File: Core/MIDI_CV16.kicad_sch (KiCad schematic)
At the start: 106 parts, among them J1 USB_C_Receptacle_USB2.0, J2 Conn_01x06_Male, J3 Conn_01x10_Female, J5 Conn_01x04, J7 Conn_01x10_Female, SW1 SW_Push_DPDT, U1 ATSAMD21G17D, U10 TL072, U11 TL072, U12 TL072, U13 MCP2517FD-xSL, U14 TLE9250V, U2 CD4052, U4 TL072, U5 TL072, U6 TL072, U7 TL072, U8 CD4052, U9 TL072, Y1 20MHz

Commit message: Update PCBs to V3.0
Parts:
- removed C10, C11, C12, C13, C14, C15, C17, C18, C19, C20, C21, C22, C23, C24, C4, C6, C7, C8, C9: 100nF, Capacitor_SMD:C_0603_1608Metric, symbol Device:C
- removed J3, J7: Conn_01x10_Female, Custom_FP:PinSocket_1x10_P2.54mm_Vertical_SMD_Pin1Both, symbol Connector:Conn_01x10_Socket
- removed R10, R13, R15, R18, R20, R21, R33, R36, R38, R40, R42, R44, R46, R48, R6, R8: 200k, Resistor_SMD:R_0603_1608Metric, symbol Device:R
- removed R11, R14, R17, R19, R25, R32, R34, R37, R39, R41, R43, R45, R47, R5, R7, R9: 68k, Resistor_SMD:R_0603_1608Metric, symbol Device:R
- removed R12, R16, R51, R52: 16k, Resistor_SMD:R_0603_1608Metric, symbol Device:R
- removed R22, R23, R26, R27, R29, R30, R31, R35, R49, R50, R53, R54, R55, R56, R57, R58: 110k, Resistor_SMD:R_0603_1608Metric, symbol Device:R
- removed U1: ATSAMD21G17D, Package_QFP:TQFP-48_7x7mm_P0.5mm, symbol MCU_Microchip_SAMD:ATSAMD21G17D-A
- removed U10, U11, U12, U4, U5, U6, U7, U9: TL072, Package_SO:SOIC-8_3.9x4.9mm_P1.27mm, symbol Amplifier_Operational:TL072
- removed U2, U8: CD4052, Package_SO:SOIC-16_3.9x9.9mm_P1.27mm, symbol Analog_Switch:CD4052B
- added C54, C55: 100nF, Capacitor_SMD:C_0603_1608Metric, symbol Device:C
- added C60, C61: 27pF, Capacitor_SMD:C_0603_1608Metric, symbol Device:C
- added R61, R62: 27.4, Resistor_SMD:R_0603_1608Metric, symbol Device:R
- added R64, R66: 1k, Resistor_SMD:R_0603_1608Metric, symbol Device:R
- added R65: NC, Resistor_SMD:R_0603_1608Metric, symbol Device:R
- added SW2, SW3: SW_SPST, Custom_FP:Tactile_angled_5x5.4_SMD, symbol Switch:SW_SPST
- added U1: RP2040, Package_DFN_QFN:QFN-56-1EP_7x7mm_P0.4mm_EP3.2x3.2mm, symbol MCU_RaspberryPi:RP2040
- added U16: CAT25640, Package_SO:SO-8_3.9x4.9mm_P1.27mm, symbol Memory_EEPROM:CAT250xxx
- added U17: IS25LP032D, Package_SO:SOIC-8_3.9x4.9mm_P1.27mm, symbol Memory_Flash:AT25SF081-SSHD-X
- added Y2: ECS-120-18-33-JGN-TR3, Crystal:Crystal_SMD_3225-4Pin_3.2x2.5mm_HandSoldering, symbol Device:Crystal_GND24
- C1: value 100nF -> 1µF
- J2: footprint Connector_PinHeader_2.54mm:PinHeader_2x03_P2.54mm_Vertical_SMD -> Custom_FP:TSM103-DH
- J5: footprint Custom_FP:MicroMatch_04_Vertical_SMD -> Custom_FP:MicroMatch_04_Vertical_SMD_Lock
- R28, R59: value 56 -> 62
- R4: value 10k -> NC
- R60: value 1k -> NC
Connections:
- net +3V3: now also R65.1, U1.1 (IOVDD), U1.10 (IOVDD), U1.22 (IOVDD), U1.33 (IOVDD), U1.42 (IOVDD), U1.43 (ADC_AVDD), U1.44 (VREG_IN), U1.48 (USB_VDD), U1.49 (IOVDD), U16.3 (~{WP}), U16.7 (~{HOLD}), U16.8 (VCC), U17.8 (VCC)
- net Butt1: now also U1.4 (GPIO2)
- net Butt2: now also U1.3 (GPIO1)
- net Butt3: now also U1.2 (GPIO0)
- net CAN_INT: now also U1.36 (GPIO24)
- net GND: now also C54.2, C55.2, C60.1, C61.1, SW2.1 (A), SW3.1 (A), U1.19 (TESTEN), U1.57 (GND), U16.4 (GND), U17.4 (GND), Y2.2, Y2.4
- net LEDC1: now also U1.15 (GPIO12)
- net LEDC2: now also U1.16 (GPIO13)
- net LEDC3: now also U1.17 (GPIO14)
- net LEDC4: now also U1.18 (GPIO15)
- net LEDC5: now also U1.28 (GPIO17)
- net LEDC6: now also U1.29 (GPIO18)
- net LEDC7: now also U1.30 (GPIO19)
- net LEDC8: now also U1.37 (GPIO25)
- net LEDR1: now also U1.41 (GPIO29_ADC3)
- net LEDR2: now also U1.40 (GPIO28_ADC2)
- net LEDR3: now also U1.39 (GPIO27_ADC1)
- net LEDR4: now also U1.38 (GPIO26_ADC0)
- net LEDR5: now also U1.27 (GPIO16)
- net MUX_A: now also U1.7 (GPIO5)
- net MUX_B: now also U1.6 (GPIO4)
- net MUX_INH: now also U1.8 (GPIO6)
- net RESET: now also SW3.2 (B), U1.26 (RUN)
- net SPI_MISO: now also U1.11 (GPIO8), U16.2 (MISO); no longer U13.12 (SDO)
- net SPI_MOSI: now also U1.14 (GPIO11), U16.5 (MOSI); no longer U13.11 (SDI)
- net SPI_SCK: now also U1.13 (GPIO10), U16.6 (SCK); no longer U13.10 (SCK)
- net SWCLK: now also U1.24 (SWCLK)
- net SWDIO: now also U1.25 (SWD)
- net USB_D+: now also R61.1
- net USB_D-: now also R62.2
- net at C3.1: now also C54.1, C55.1, U1.23 (DVDD), U1.45 (VREG_VOUT), U1.50 (DVDD)
- net MIDIBUS+ renamed M2IDI+
- net MIDIBUS- renamed M2IDI-
- net SPI_SS renamed CAN_CS
- net CAN_CS: now also U1.32 (GPIO21)
- new net: C60.2, R66.1, Y2.1
- new net: R66.2, U1.21 (XOUT)
- new net: R64.2, SW2.2 (B)
- new net: C61.2, U1.20 (XIN), Y2.3
- new net CAN_MISO: U1.31 (GPIO20), U13.12 (SDO)
- new net CAN_MOSI: U1.35 (GPIO23), U13.11 (SDI)
- new net CAN_SCK: U1.34 (GPIO22), U13.10 (SCK)
- new net DAC_CS: U1.9 (GPIO7)
- new net EEPROM_CS: U1.12 (GPIO9), U16.1 (~{CS})
- new net FLASH_CS: R64.1, R65.2, U1.56 (QSPI_SS), U17.1 (~{CS})
- new net FLASH_SCK: U1.52 (QSPI_SCLK), U17.6 (SCK)
- new net FLASH_SD0: U1.53 (QSPI_SD0), U17.5 (SI/IO0)
- new net FLASH_SD1: U1.55 (QSPI_SD1), U17.2 (SO/IO1)
- new net FLASH_SD2: U1.54 (QSPI_SD2), U17.3 (~{WP}/IO2)
- new net FLASH_SD3: U1.51 (QSPI_SD3), U17.7 (~{HOLD}/IO3)
- new net MCU_USB_D+: R61.2, U1.47 (USB_DP)
- new net MCU_USB_D-: R62.1, U1.46 (USB_DM)
- no-connect marks 4 -> 5
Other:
- added sheet Outputs (Outputs.kicad_sch)
- note removed: "31k"
- note removed: "47k"
- note removed: "91k"
- note removed: "TxD on SERCOM[0] or SERCOM[2]"
- moved on the sheet: C3, J2, R4, R60

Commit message: Shrink crystal fp and add silkscreen text
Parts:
- Y2: footprint Crystal:Crystal_SMD_3225-4Pin_3.2x2.5mm_HandSoldering -> Custom_FP:Crystal_SMD_3225-4Pin_3.2x2.5mm_HandSoldering
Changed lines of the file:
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@@
       (effects (font (size 1.27 1.27)))
     )
-    (property "Footprint" "Crystal:Crystal_SMD_3225-4Pin_3.2x2.5mm_HandSoldering" (at 85.725 139.065 0)
+    (property "Footprint" "Custom_FP:Crystal_SMD_3225-4Pin_3.2x2.5mm_HandSoldering" (at 85.725 139.065 0)
       (effects (font (size 1.27 1.27)) hide)
     )

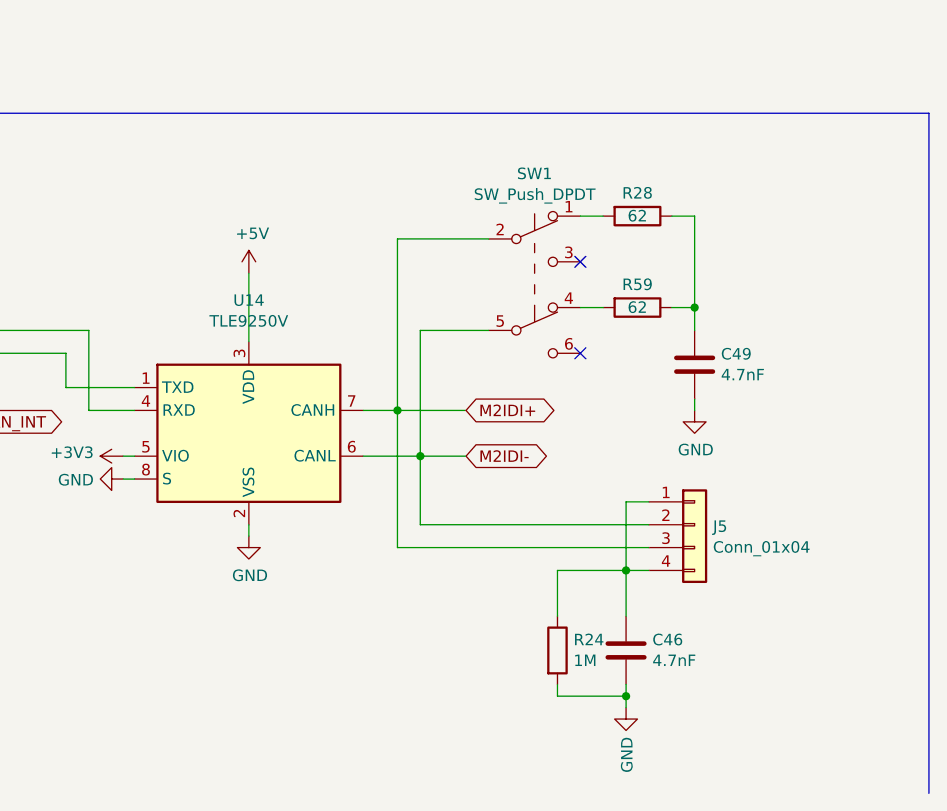
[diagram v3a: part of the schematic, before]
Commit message: Change CAN tranceiver to MCP2562
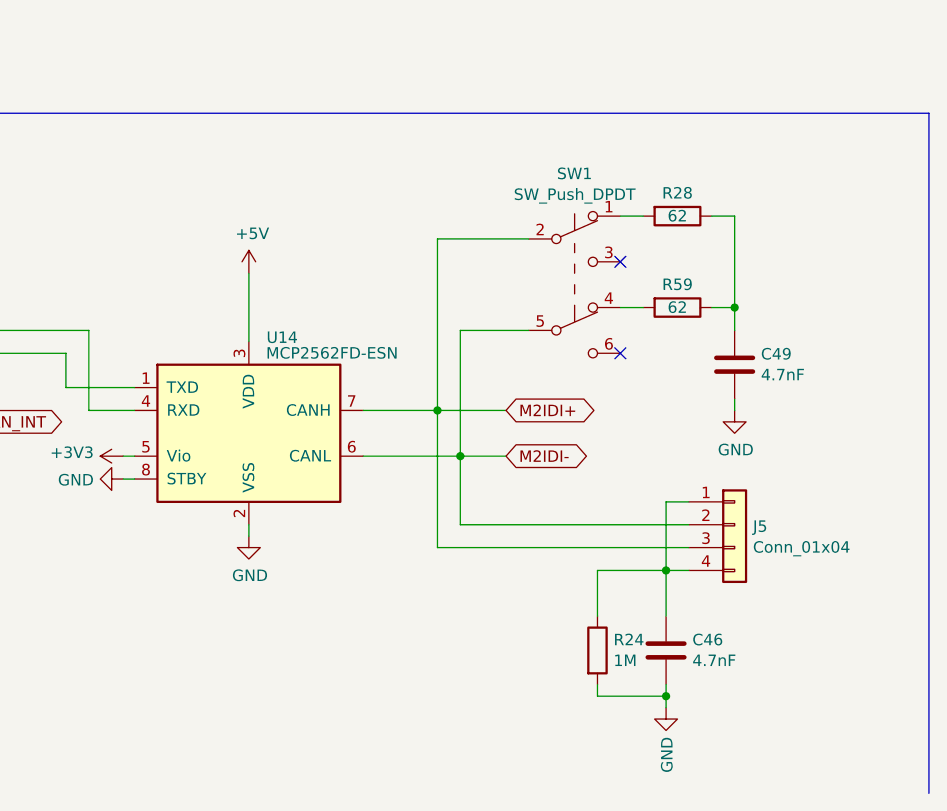
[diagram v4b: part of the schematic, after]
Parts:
- removed U14: TLE9250V, Package_SO:Infineon_PG-DSO-8-27_3.9x4.9mm_EP2.65x3mm, symbol Interface_CAN_LIN:MCP2558FD-xMF
- added U14: MCP2562FD-ESN, Package_SO:SOIC-8_3.9x4.9mm_P1.27mm, symbol Interface_CAN_LIN:MCP2562-E-SN
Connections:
- net +3V3: now also U14.5 (Vio)
- net +5V: now also U14.3 (VDD)
- net GND: now also U14.2 (VSS), U14.8 (STBY)
- net M2IDI+: now also U14.7 (CANH)
- net M2IDI-: now also U14.6 (CANL)
- net at U13.1 (TXCAN): now also U14.1 (TXD)
- net at U13.2 (RXCAN): now also U14.4 (RXD)
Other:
- moved on the sheet: C46, C49, J5, R24, R28, R59, SW1

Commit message: Finalize module
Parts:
- R28, R59: footprint Resistor_SMD:R_0603_1608Metric -> Resistor_SMD:R_0805_2012Metric
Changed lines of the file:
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@@
       (effects (font (size 1.27 1.27)))
     )
-    (property "Footprint" "Resistor_SMD:R_0603_1608Metric" (at 244.475 229.362 90)
+    (property "Footprint" "Resistor_SMD:R_0805_2012Metric" (at 244.475 229.362 90)
       (effects (font (size 1.27 1.27)) hide)
     )
@@
       (effects (font (size 1.27 1.27)))
     )
-    (property "Footprint" "Resistor_SMD:R_0603_1608Metric" (at 244.475 219.202 90)
+    (property "Footprint" "Resistor_SMD:R_0805_2012Metric" (at 244.475 219.202 90)
       (effects (font (size 1.27 1.27)) hide)
     )

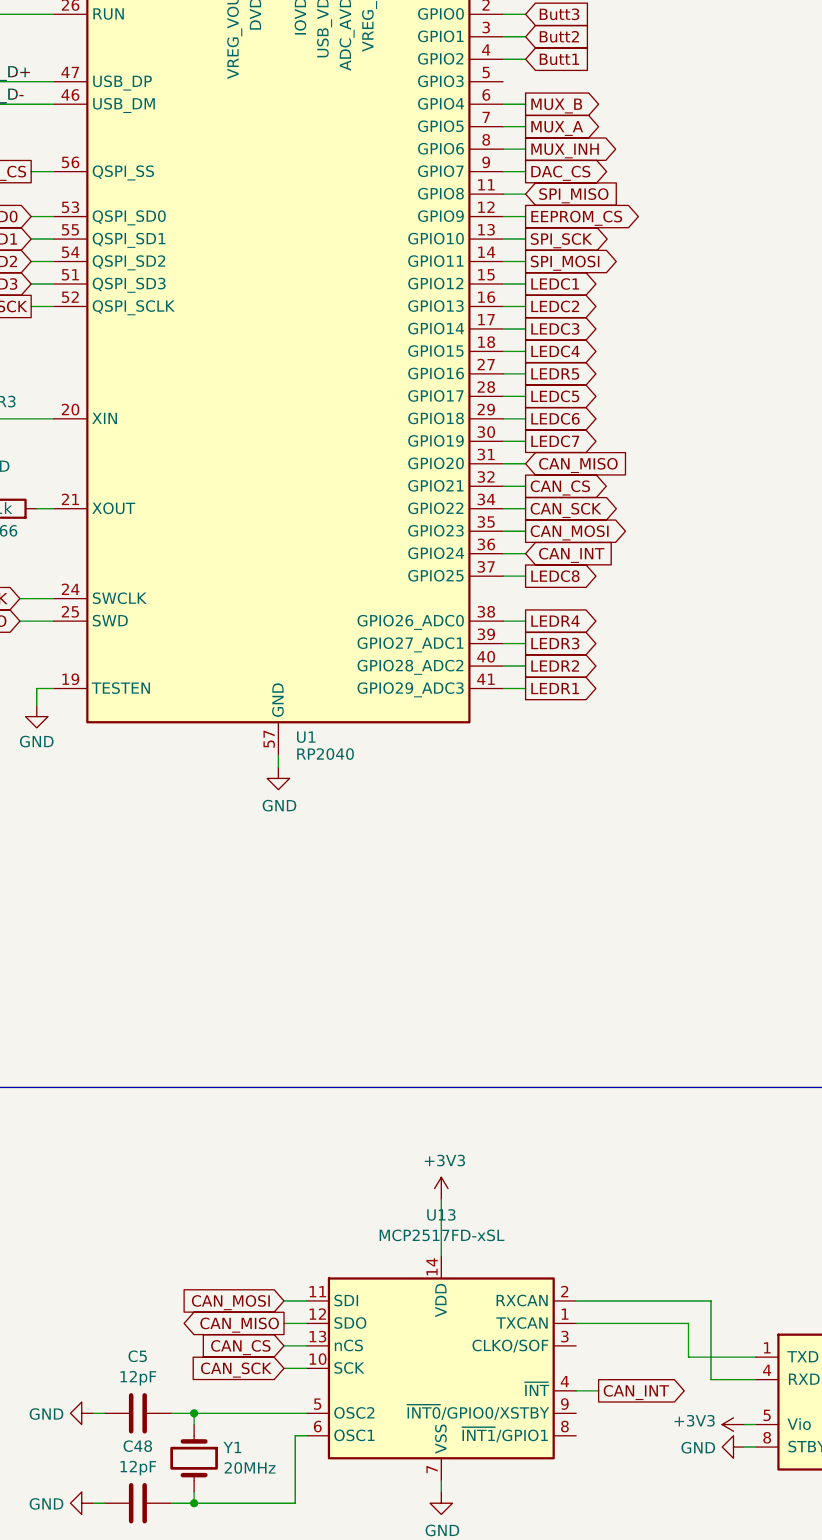
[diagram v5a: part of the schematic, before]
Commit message: Change SPI bus for EEPROM
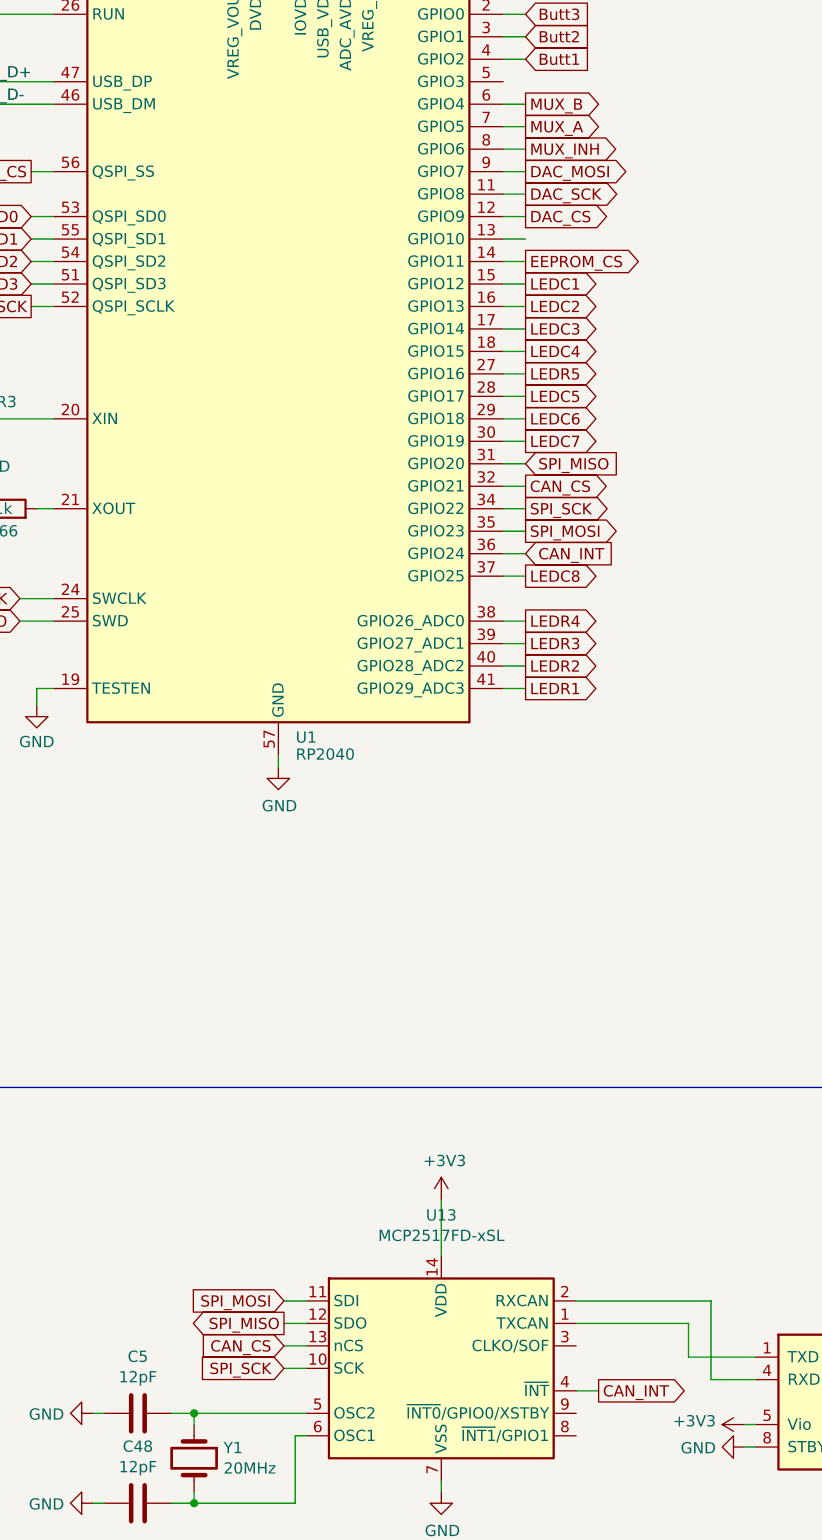
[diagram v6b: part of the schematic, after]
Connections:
- net CAN_MISO is gone; now on net SPI_MISO: U1.31 (GPIO20), U13.12 (SDO)
- net CAN_MOSI is gone; now on net SPI_MOSI: U1.35 (GPIO23), U13.11 (SDI)
- net CAN_SCK is gone; now on net SPI_SCK: U1.34 (GPIO22), U13.10 (SCK)
- net DAC_CS: now also U1.12 (GPIO9); no longer U1.9 (GPIO7)
- net EEPROM_CS: now also U1.14 (GPIO11); no longer U1.12 (GPIO9)
- net SPI_MISO: no longer U1.11 (GPIO8)
- net SPI_MOSI: no longer U1.14 (GPIO11)
- net SPI_SCK: no longer U1.13 (GPIO10)
- new net DAC_MOSI: U1.9 (GPIO7)
- new net DAC_SCK: U1.11 (GPIO8)
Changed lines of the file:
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@@
     (effects (font (size 1.27 1.27)) (justify left bottom))
   )
-  (global_label "SPI_SCK" (shape output) (at 158.115 113.665 0) (fields_autoplaced)
-    (effects (font (size 1.27 1.27)) (justify left))
-    (property "Intersheetrefs" "${INTERSHEET_REFS}" (at 168.168 113.665 0)
+  (global_label "DAC_SCK" (shape output) (at 158.115 108.585 0) (fields_autoplaced)
+    (effects (font (size 1.27 1.27)) (justify left))
+    (property "Intersheetrefs" "${INTERSHEET_REFS}" (at 168.7917 108.585 0)
       (effects (font (size 1.27 1.27)) (justify left) hide)
     )
@@
     )
   )
-  (global_label "SPI_MISO" (shape input) (at 158.115 108.585 0) (fields_autoplaced)
-    (effects (font (size 1.27 1.27)) (justify left))
-    (property "Intersheetrefs" "${INTERSHEET_REFS}" (at 169.0147 108.585 0)
-      (effects (font (size 1.27 1.27)) (justify left) hide)
-    )
-  )
   (global_label "SWDIO" (shape output) (at 35.56 192.405 180)
     (effects (font (size 1.27 1.27)) (justify right))
@@
     )
   )
-  (global_label "DAC_CS" (shape output) (at 158.115 106.045 0) (fields_autoplaced)
-    (effects (font (size 1.27 1.27)) (justify left))
-    (property "Intersheetrefs" "${INTERSHEET_REFS}" (at 167.4423 106.045 0)
-      (effects (font (size 1.27 1.27)) (justify left) hide)
-    )
-  )
-  (global_label "CAN_MISO" (shape output) (at 130.81 236.22 180)
+  (global_label "DAC_CS" (shape output) (at 158.115 111.125 0) (fields_autoplaced)
+    (effects (font (size 1.27 1.27)) (justify left))
+    (property "Intersheetrefs" "${INTERSHEET_REFS}" (at 167.4423 111.125 0)
+      (effects (font (size 1.27 1.27)) (justify left) hide)
+    )
+  )
+  (global_label "SPI_MISO" (shape output) (at 130.81 236.22 180)
     (effects (font (size 1.27 1.27)) (justify right))
     (property "Intersheetrefs" "${INTERSHEET_REFS}" (at 130.81 236.22 0)
@@
     )
   )
-  (global_label "CAN_MOSI" (shape input) (at 130.81 233.68 180)
+  (global_label "SPI_MOSI" (shape input) (at 130.81 233.68 180)
     (effects (font (size 1.27 1.27)) (justify right))
     (property "Intersheetrefs" "${INTERSHEET_REFS}" (at 130.81 233.68 0)
@@
     )
   )
-  (global_label "EEPROM_CS" (shape output) (at 158.115 111.125 0) (fields_autoplaced)
-    (effects (font (size 1.27 1.27)) (justify left))
-    (property "Intersheetrefs" "${INTERSHEET_REFS}" (at 171.4336 111.125 0)
+  (global_label "EEPROM_CS" (shape output) (at 158.115 116.205 0) (fields_autoplaced)
+    (effects (font (size 1.27 1.27)) (justify left))
+    (property "Intersheetrefs" "${INTERSHEET_REFS}" (at 171.4336 116.205 0)
       (effects (font (size 1.27 1.27)) (justify left) hide)
     )
@@
     )
   )
-  (global_label "CAN_SCK" (shape input) (at 130.81 241.3 180)
+  (global_label "SPI_SCK" (shape input) (at 130.81 241.3 180)
     (effects (font (size 1.27 1.27)) (justify right))
     (property "Intersheetrefs" "${INTERSHEET_REFS}" (at 130.81 241.3 0)
@@
     )
   )
-  (global_label "CAN_MISO" (shape input) (at 158.115 139.065 0)
+  (global_label "SPI_MISO" (shape input) (at 158.115 139.065 0)
     (effects (font (size 1.27 1.27)) (justify left))
     (property "Intersheetrefs" "${INTERSHEET_REFS}" (at 158.115 139.065 0)
@@
     )
   )
-  (global_label "SPI_MOSI" (shape output) (at 158.115 116.205 0) (fields_autoplaced)
-    (effects (font (size 1.27 1.27)) (justify left))
-    (property "Intersheetrefs" "${INTERSHEET_REFS}" (at 169.0147 116.205 0)
+  (global_label "DAC_MOSI" (shape output) (at 158.115 106.045 0) (fields_autoplaced)
+    (effects (font (size 1.27 1.27)) (justify left))
+    (property "Intersheetrefs" "${INTERSHEET_REFS}" (at 169.6384 106.045 0)
       (effects (font (size 1.27 1.27)) (justify left) hide)
     )
@@
     )
   )
-  (global_label "CAN_MOSI" (shape output) (at 158.115 146.685 0)
+  (global_label "SPI_MOSI" (shape output) (at 158.115 146.685 0)
     (effects (font (size 1.27 1.27)) (justify left))
     (property "Intersheetrefs" "${INTERSHEET_REFS}" (at 158.115 146.685 0)
@@
     )
   )
-  (global_label "CAN_SCK" (shape output) (at 158.115 144.145 0)
+  (global_label "SPI_SCK" (shape output) (at 158.115 144.145 0)
     (effects (font (size 1.27 1.27)) (justify left))
     (property "Intersheetrefs" "${INTERSHEET_REFS}" (at 158.115 144.145 0)

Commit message: Layout v3.1
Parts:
- SW2, SW3: footprint Custom_FP:Tactile_angled_5x5.4_SMD -> Custom_FP:Tactile_angled_SPST_5x5.4_SMD
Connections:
- net CAN_CS: now also U1.37 (GPIO25); no longer U1.32 (GPIO21)
- net DAC_CS: now also U1.16 (GPIO13); no longer U1.12 (GPIO9)
- net DAC_MOSI: now also U1.14 (GPIO11); no longer U1.9 (GPIO7)
- net DAC_SCK: now also U1.15 (GPIO12); no longer U1.11 (GPIO8)
- net EEPROM_CS: now also U1.5 (GPIO3); no longer U1.14 (GPIO11)
- net LEDC1: now also U1.17 (GPIO14); no longer U1.15 (GPIO12)
- net LEDC2: now also U1.27 (GPIO16); no longer U1.16 (GPIO13)
- net LEDC3: now also U1.28 (GPIO17); no longer U1.17 (GPIO14)
- net LEDC4: now also U1.29 (GPIO18); no longer U1.18 (GPIO15)
- net LEDC5: now also U1.31 (GPIO20); no longer U1.28 (GPIO17)
- net LEDC6: now also U1.32 (GPIO21); no longer U1.29 (GPIO18)
- net LEDC7: now also U1.34 (GPIO22); no longer U1.30 (GPIO19)
- net LEDC8: now also U1.35 (GPIO23); no longer U1.37 (GPIO25)
- net LEDR5: now also U1.30 (GPIO19); no longer U1.27 (GPIO16)
- net MUX_A: now also U1.11 (GPIO8); no longer U1.7 (GPIO5)
- net MUX_B: now also U1.12 (GPIO9); no longer U1.6 (GPIO4)
- net MUX_INH: now also U1.13 (GPIO10); no longer U1.8 (GPIO6)
- net SPI_MISO: now also U1.6 (GPIO4); no longer U1.31 (GPIO20)
- net SPI_MOSI: now also U1.9 (GPIO7); no longer U1.35 (GPIO23)
- net SPI_SCK: now also U1.8 (GPIO6); no longer U1.34 (GPIO22)
